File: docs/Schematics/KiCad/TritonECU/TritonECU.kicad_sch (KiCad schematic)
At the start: 0 parts

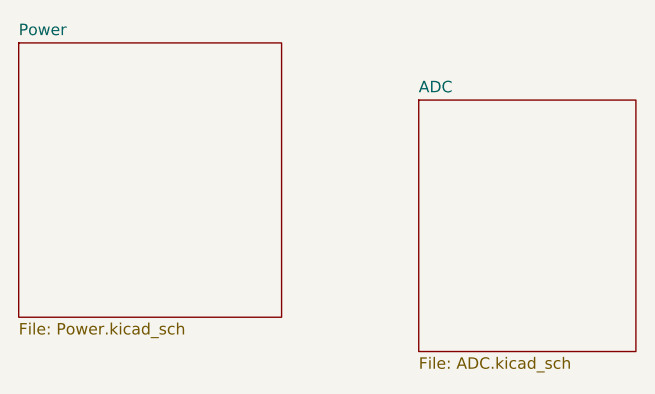
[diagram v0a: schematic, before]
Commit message: Add TritonECU-Main carrier floor plan with F767 MCU module
New KiCad project for the main (carrier) board. The EEC-V 104-pin connector
uses rusEFI geometry with TE pin drill and edge distance. The power board V3
and VR board V1 mates are read from their own PCB/gerbers. The Nucleo-144 is
replaced by a 44 x 44 mm STM32F767ZIT6 module (DB3) on 10 mm M3 standoffs
with four 2x18 1.27 mm headers breaking out all 110 port pins.
mcu_pinout.py is the module pinout's source of truth.

The ADC sheet moves from the power project to the main project.

Co-Authored-By: Claude Opus 5.5 <noreply@anthropic.com>
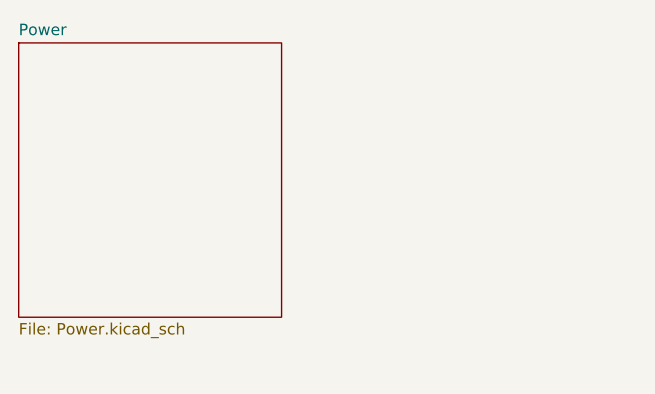
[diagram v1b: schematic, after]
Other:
- removed sheet ADC
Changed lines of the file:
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@@
-		)
-	)
-	(sheet
-		(at 71.12 30.48)
-		(size 24.13 27.94)
-		(exclude_from_sim no)
-		(in_bom yes)
-		(on_board yes)
-		(dnp no)
-		(fields_autoplaced yes)
-		(stroke
-			(width 0.1524)
-			(type solid)
-		)
-		(fill
-			(color 0 0 0 0)
-		)
-		(property "Sheetname" "ADC"
-			(at 71.12 29.7684 0)
-			(show_name no)
-			(do_not_autoplace no)
-			(effects
-				(font
-					(size 1.27 1.27)
-				)
-				(justify left bottom)
-			)
-		)
-		(property "Sheetfile" "ADC.kicad_sch"
-			(at 71.12 59.0046 0)
-			(show_name no)
-			(do_not_autoplace no)
-			(effects
-				(font
-					(size 1.27 1.27)
-				)
-				(justify left top)
-			)
-		)
-		(instances
-			(project "TritonECU"
-				(path "/6415d7cc-f88c-411d-b71d-6233e8c6ab9d"
-					(page "3")
-				)
-			)
 		)
 	)
